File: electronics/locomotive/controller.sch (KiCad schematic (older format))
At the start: 26 parts, among them U1 STM32F405RGTx, Y1 16MHz

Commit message: electronics: locomotive: Board Rev 1.0
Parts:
- removed R4: 13k2, symbol R_Small
- removed R5: 2k8, symbol R_Small
- removed R6, R7: R, symbol R_Small
- removed R8, R9: 4k7, symbol R_Small
- added JP3: VCAP1, bcan:Solder_Jumper_NO, symbol Jumper_NO_Small
- added JP4: VCAP2, bcan:Solder_Jumper_NO, symbol Jumper_NO_Small
- C1, C10, C11, C12, C2, C3, C4, C5, C6, C7, C8, C9, L1: footprint (none) -> Capacitors_SMD:C_0603
- JP1, JP2: footprint (none) -> bcan:Solder_Jumper_NC
- R1, R2, R3: footprint (none) -> Resistors_SMD:R_0603
- U1: footprint LQFP64 -> Housings_QFP:TQFP-64_10x10mm_Pitch0.5mm
- Y1: footprint (none) -> Crystals:Crystal_SMD_3225-4pin_3.2x2.5mm
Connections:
- net labels added: VDDA
- net labels removed: BOOT1, DCC_IN, I2C2_SCL, I2C2_SDA, IR_L, IR_R, JTAG_RST, JTAG_TCK, JTAG_TDI, JTAG_TDO, JTAG_TMS, PA[0..15], PB[0..15], PC[0..15], PWM_A, PWM_B, SPI2_MISO, SPI2_MOSI, SPI2_NSS, SPI2_SCK, USB_D+, USB_D-, USB_ID, USB_VBUS, VCC, VMOT
- wire segments 151 -> 48
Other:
- moved on the sheet: C1, C10, C11, C12, C2, C3, C4, C5, C6, C7, C8, C9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

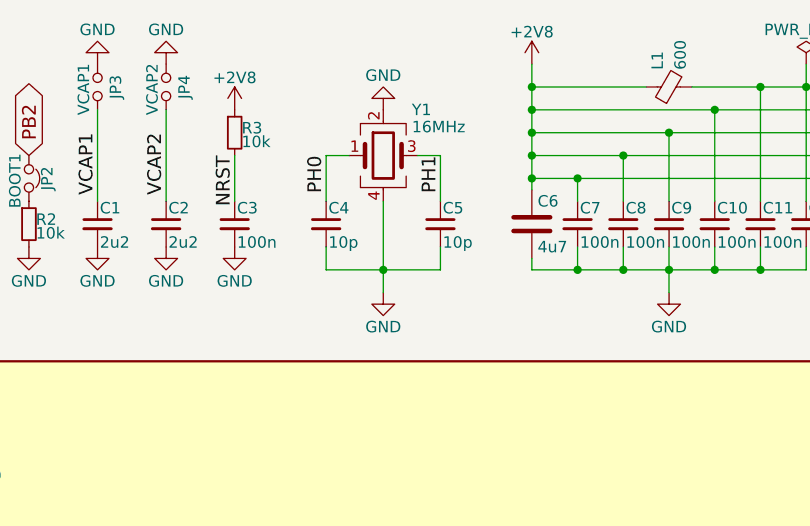
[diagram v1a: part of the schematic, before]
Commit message: electronics: locomotive: Fix mislabeled parts
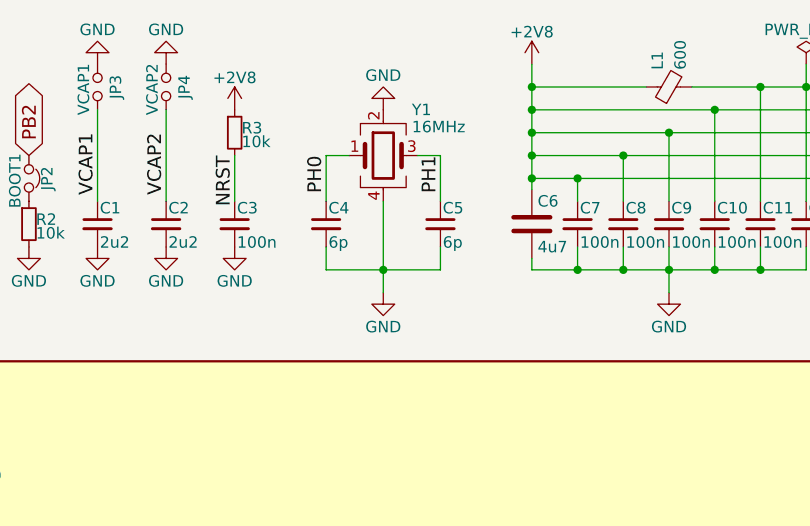
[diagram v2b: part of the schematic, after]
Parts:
- C4, C5: value 10p -> 6p
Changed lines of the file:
@@
 P 3300 1900
 F 0 "C4" H 3310 1970 50  0000 L CNN
-F 1 "10p" H 3310 1820 50  0000 L CNN
+F 1 "6p" H 3310 1820 50  0000 L CNN
 F 2 "Capacitors_SMD:C_0603" H 3300 1900 50  0001 C CNN
 F 3 "" H 3300 1900 50  0001 C CNN
@@
 P 3800 1900
 F 0 "C5" H 3810 1970 50  0000 L CNN
-F 1 "10p" H 3810 1820 50  0000 L CNN
+F 1 "6p" H 3810 1820 50  0000 L CNN
 F 2 "Capacitors_SMD:C_0603" H 3800 1900 50  0001 C CNN
 F 3 "" H 3800 1900 50  0001 C CNN
